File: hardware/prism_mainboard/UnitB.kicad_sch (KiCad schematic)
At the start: 1 part, among them U1 XC7Z010-1CLG400C

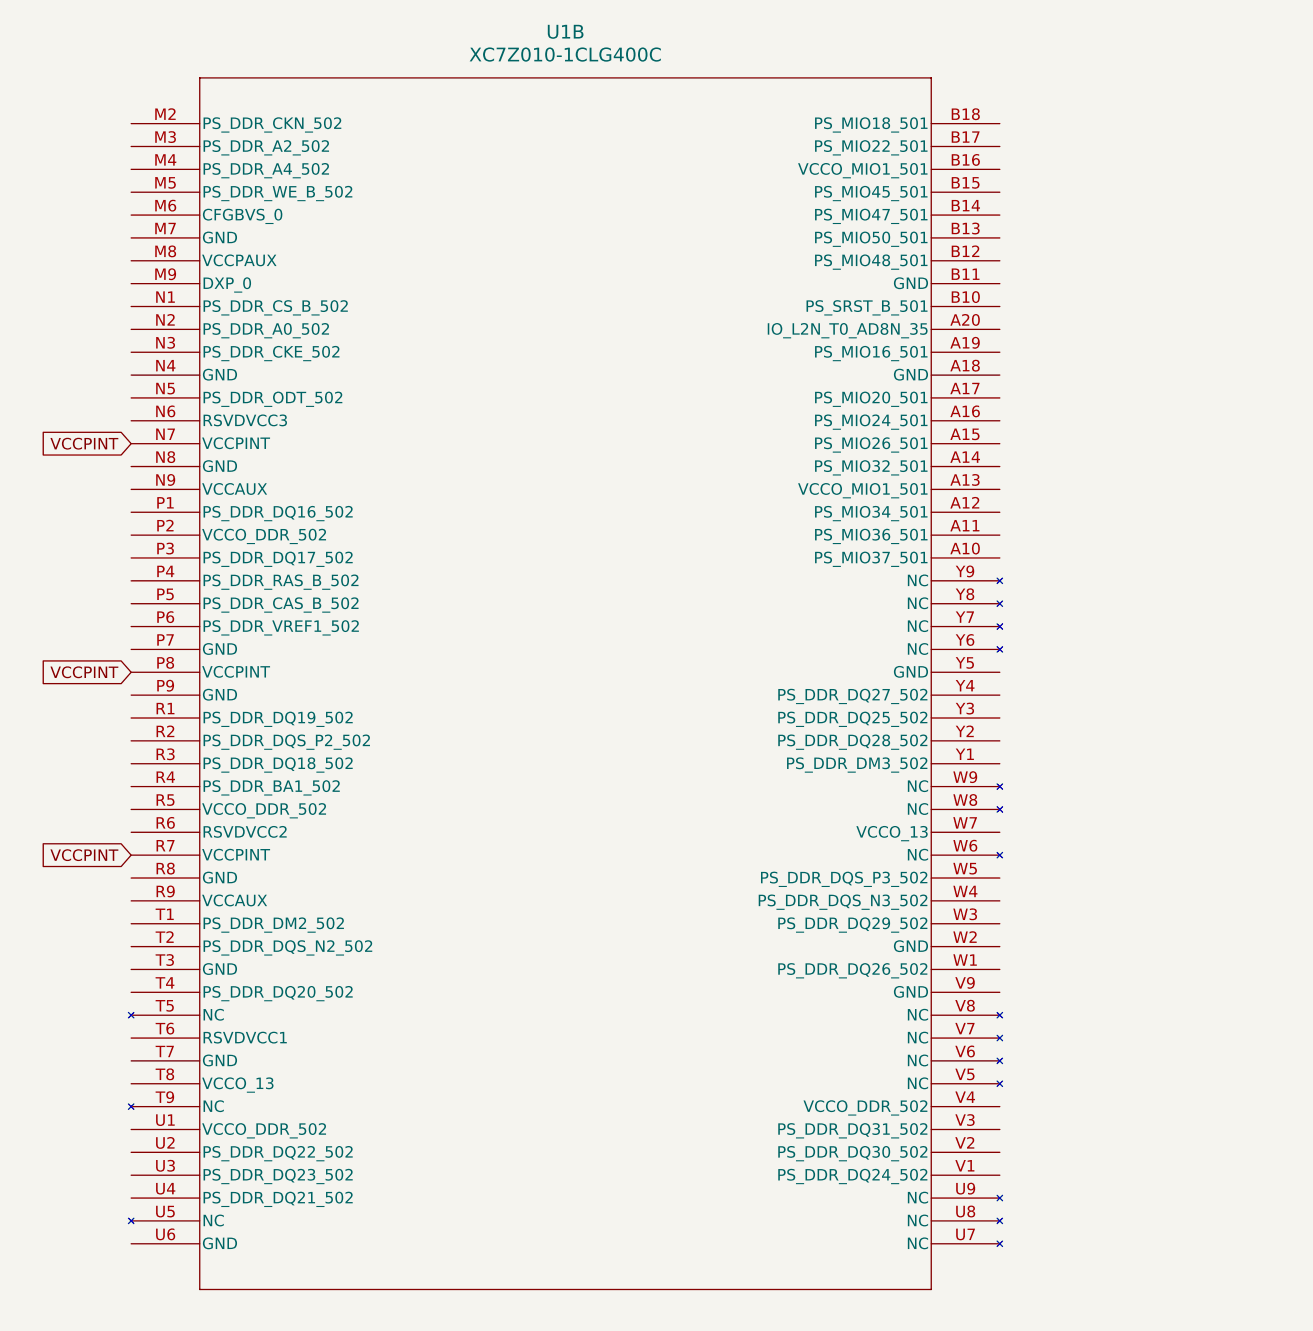
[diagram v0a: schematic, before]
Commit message: Zynq-7000 Schematic Updates
Added basic power net labels for the PL and PS portions of the FPGA.
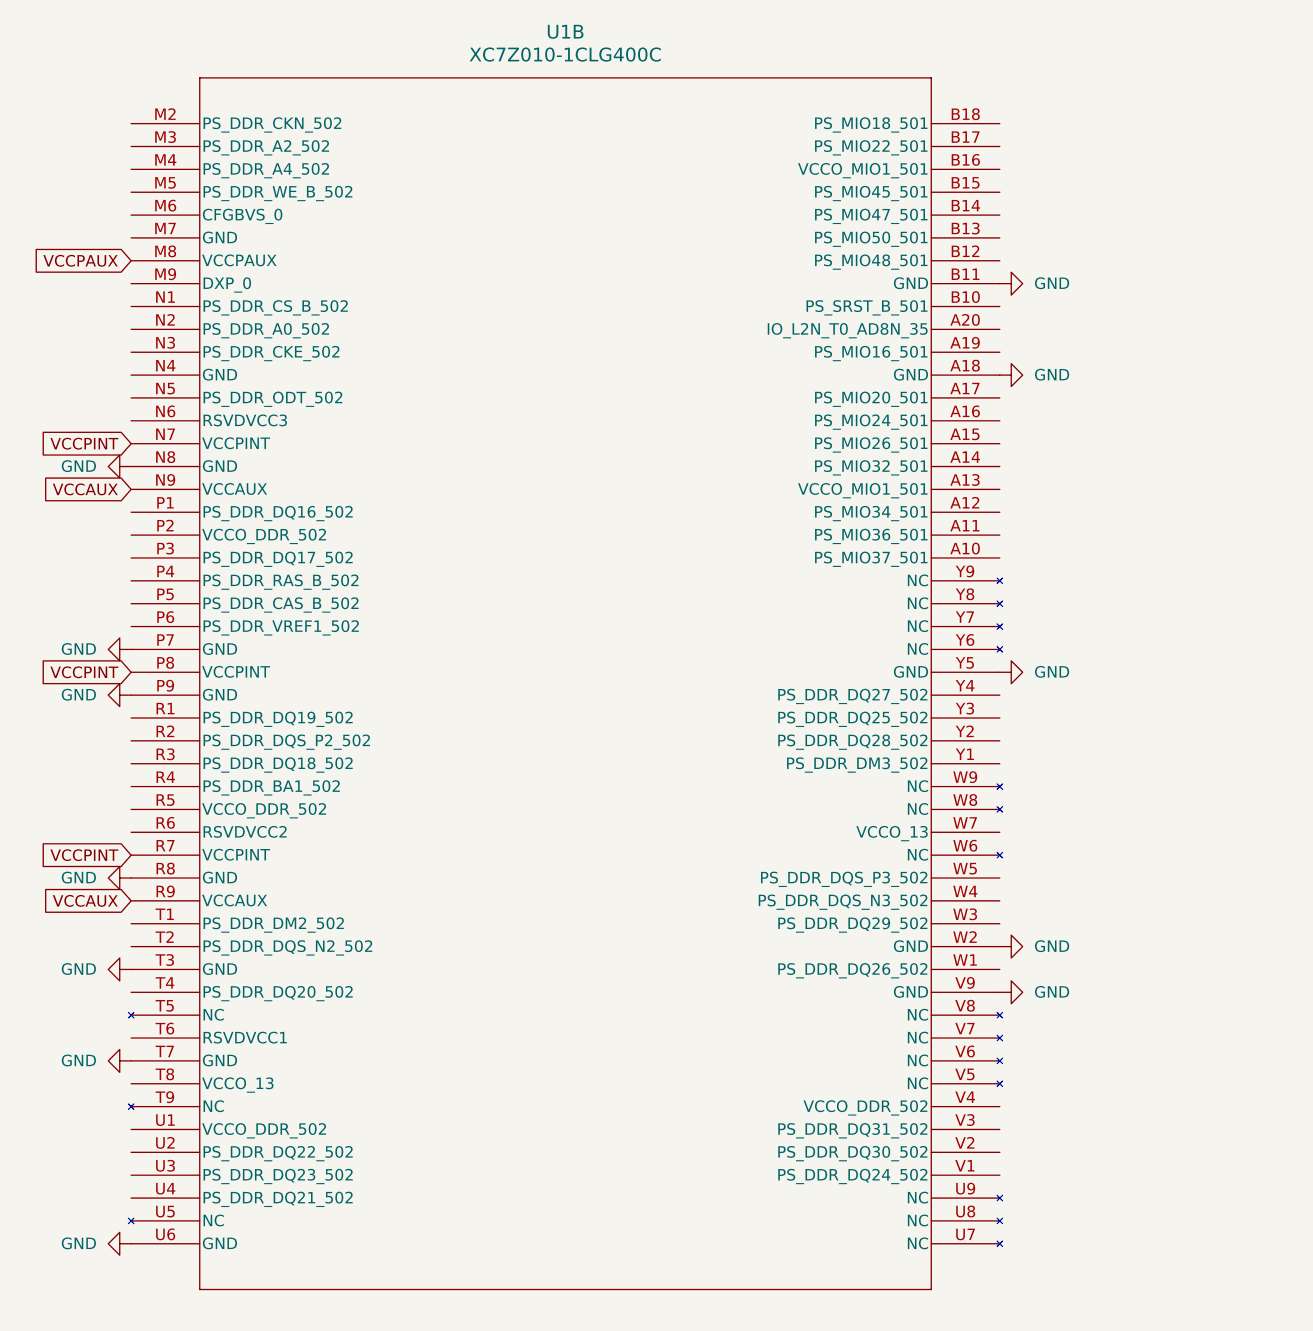
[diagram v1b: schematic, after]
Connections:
- net GND: now reaches U1.A18 (GND)
- net GND: now also U1.B11 (GND), U1.N8 (GND), U1.P7 (GND), U1.P9 (GND), U1.R8 (GND), U1.T3 (GND), U1.T7 (GND), U1.U6 (GND), U1.V9 (GND), U1.W2 (GND), U1.Y5 (GND)
- net VCCPAUX: now reaches U1.M8 (VCCPAUX)
- net VCCAUX: now reaches U1.N9 (VCCAUX)
- net VCCAUX: now also U1.R9 (VCCAUX)

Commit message: Mainboard Updates
Started a lot of the basic schematic nets like GND and Power nets. Major Change: Decided on using the XC7Z015-1CLG485I instead of the 7010 or 7020 due to the ability to use HDMI interfaces with an adapter and more LUTs. Updated schematic symbols and footprints accordingly. Added Memory, Encoder, MicroSD schematics. Added LimeSDR footprints as well. Will Try to add Power to the entire board next.
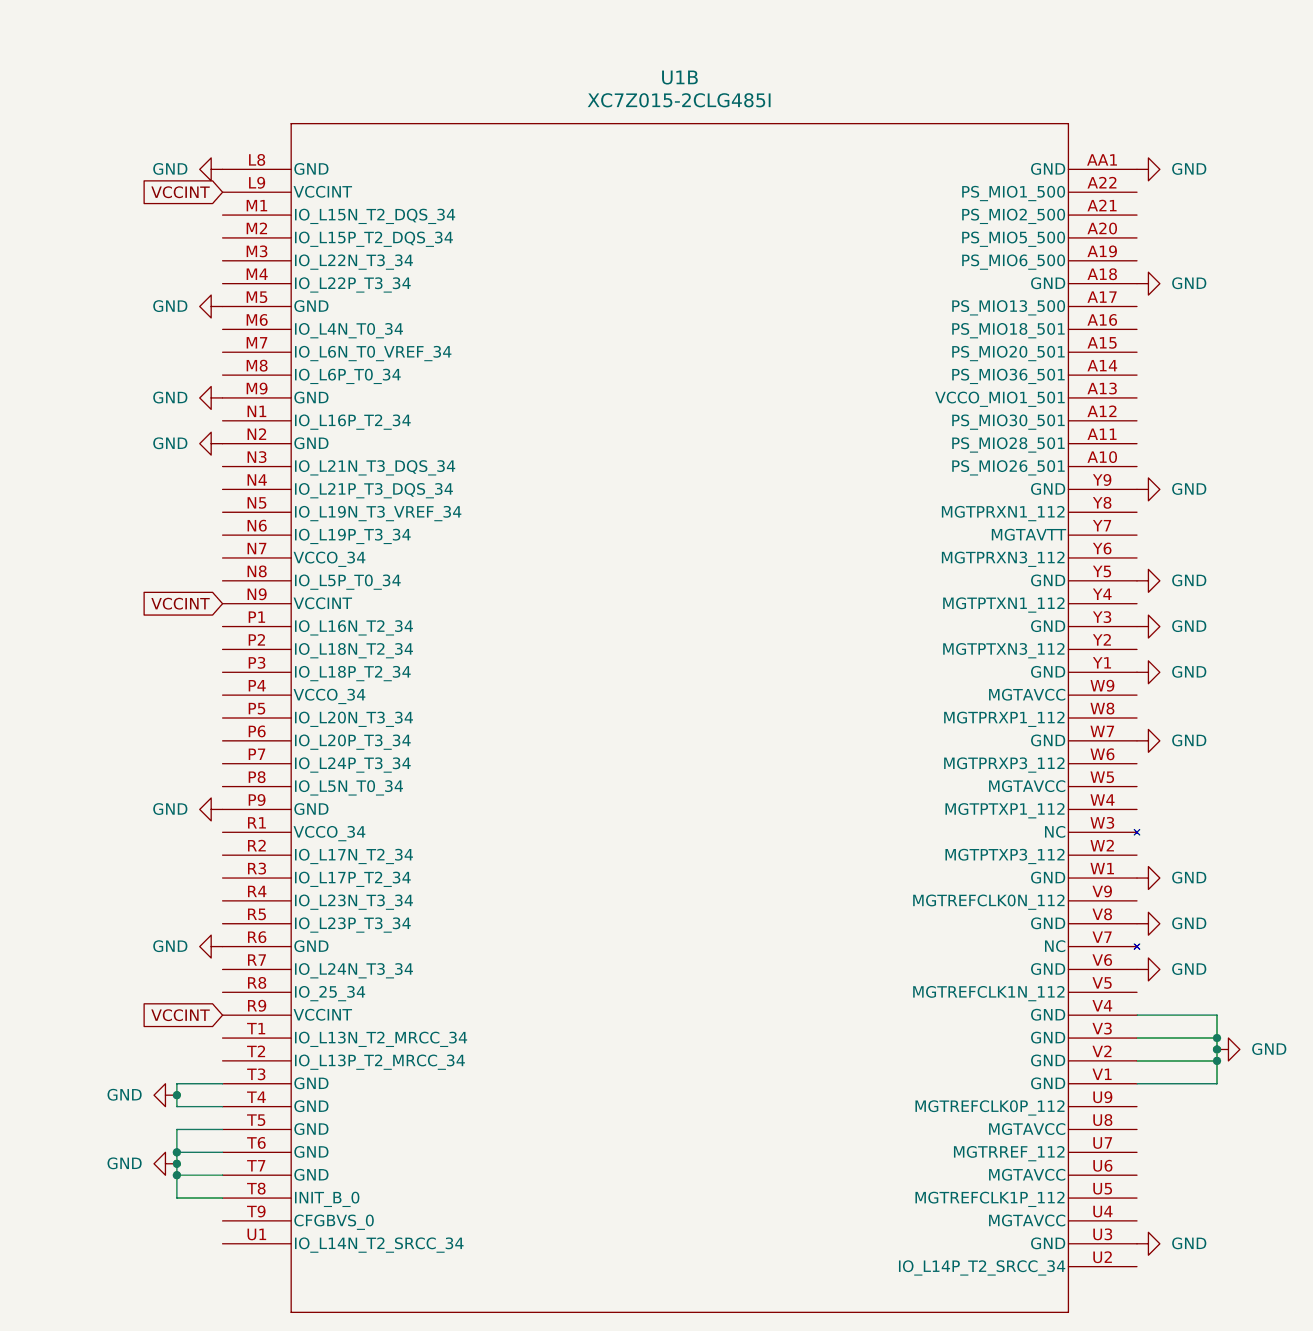
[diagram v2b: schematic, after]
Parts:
- removed U1: XC7Z010-1CLG400C, XC7Z010-1CLG400C:CLG400_XIL, symbol XC7Z010-1CLG400C:XC7Z010-1CLG400C
- added U1: XC7Z015-2CLG485I, CLG485_XIL, symbol XC7Z015-CLG485:XC7Z015-2CLG485I
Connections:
- net GND: now also U1.A18 (GND), U1.AA1 (GND), U1.L8 (GND), U1.M5 (GND), U1.M9 (GND), U1.N2 (GND), U1.P9 (GND), U1.R6 (GND), U1.T3 (GND), U1.T4 (GND), U1.T5 (GND), U1.T6 (GND), U1.T7 (GND), U1.T8 (INIT_B_0), U1.U3 (GND), U1.V1 (GND), U1.V2 (GND), U1.V3 (GND), U1.V4 (GND), U1.V6 (GND), U1.V8 (GND), U1.W1 (GND), U1.W7 (GND), U1.Y1 (GND), U1.Y3 (GND), U1.Y5 (GND), U1.Y9 (GND)
- new net VCCINT: U1.L9 (VCCINT), U1.N9 (VCCINT), U1.R9 (VCCINT)

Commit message: Schematic Updates
Updated the DDR3 DRAM to 4Gb, added a lot of nets and started updating the power and decoupling components. Updated .gitignore to avoid .mkv files.
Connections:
- net VCCO_MIO1: now reaches U1.A13 (VCCO_MIO1_501)
- net VCCO_34: now reaches U1.N7 (VCCO_34)
- net VCCO_35: now reaches U1.P4 (VCCO_34)
- net VCCO_35: now also U1.R1 (VCCO_34)
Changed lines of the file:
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@@
+		)
+	)
+	(global_label "VCCO_35"
+		(shape input)
+		(at 99.06 106.68 180)
+		(fields_autoplaced yes)
+		(effects
+			(font
+				(size 1.27 1.27)
+			)
+			(justify right)
+		)
+		(property "Intersheetrefs" "${INTERSHEET_REFS}"
+			(at 87.7291 106.68 0)
+			(hide yes)
+			(show_name no)
+			(do_not_autoplace no)
+			(effects
+				(font
+					(size 1.27 1.27)
+				)
+				(justify right)
+			)
+		)
+	)
+	(global_label "VCCO_34"
+		(shape input)
+		(at 99.06 76.2 180)
+		(fields_autoplaced yes)
+		(effects
+			(font
+				(size 1.27 1.27)
+			)
+			(justify right)
+		)
+		(property "Intersheetrefs" "${INTERSHEET_REFS}"
+			(at 87.7291 76.2 0)
+			(hide yes)
+			(show_name no)
+			(do_not_autoplace no)
+			(effects
+				(font
+					(size 1.27 1.27)
+				)
+				(justify right)
+			)
 		)
 	)
@@
 		)
 	)
+	(global_label "VCCO_MIO1"
+		(shape input)
+		(at 200.66 58.42 0)
+		(fields_autoplaced yes)
+		(effects
+			(font
+				(size 1.27 1.27)
+			)
+			(justify left)
+		)
+		(property "Intersheetrefs" "${INTERSHEET_REFS}"
+			(at 214.1681 58.42 0)
+			(hide yes)
+			(show_name no)
+			(do_not_autoplace no)
+			(effects
+				(font
+					(size 1.27 1.27)
+				)
+				(justify left)
+			)
+		)
+	)
 	(global_label "VCCINT"
 		(shape input)
@@
 			(hide yes)
 			(show_name no)
+			(do_not_autoplace no)
+			(effects
+				(font
+					(size 1.27 1.27)
+				)
+				(justify right)
+			)
+		)
+	)
+	(global_label "VCCO_35"
+		(shape input)
+		(at 99.06 91.44 180)
+		(fields_autoplaced yes)
+		(effects
+			(font
+				(size 1.27 1.27)
+			)
+			(justify right)
+		)
+		(property "Intersheetrefs" "${INTERSHEET_REFS}"
+			(at 87.7291 91.44 0)
+			(hide yes)
+			(show_name no)

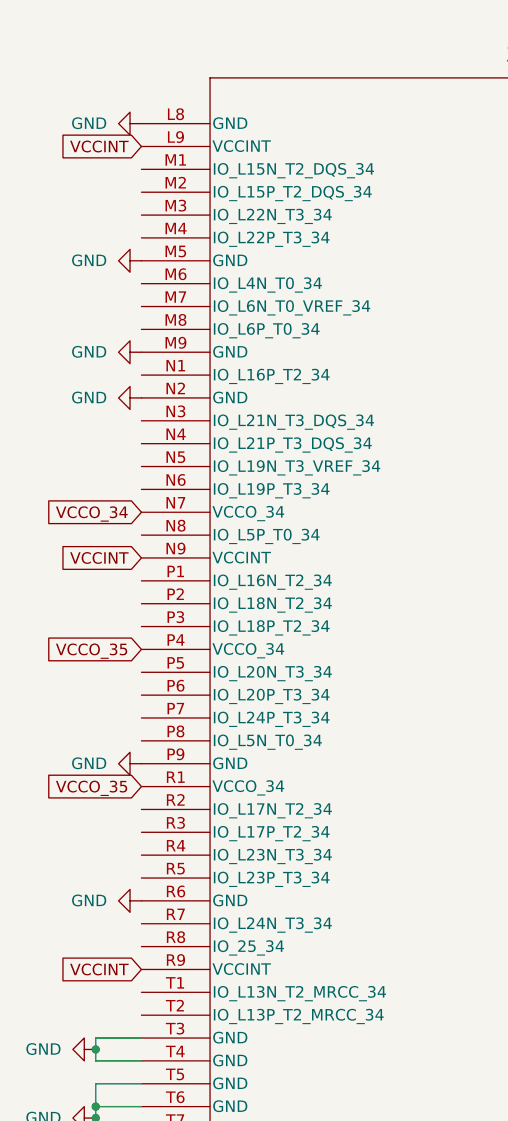
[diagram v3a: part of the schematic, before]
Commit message: Schematic Updates
Added the LMS7002M to XC7Z015 connections, atleast the preliminary data connections.
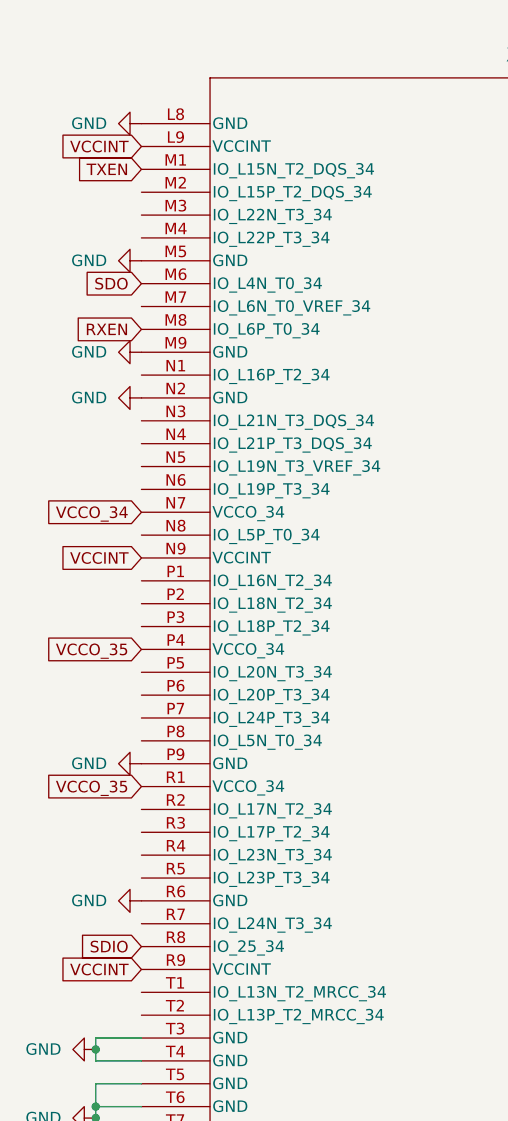
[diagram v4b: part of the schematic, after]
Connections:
- net TXEN: now reaches U1.M1 (IO_L15N_T2_DQS_34)
- net SDO: now reaches U1.M6 (IO_L4N_T0_34)
- net RXEN: now reaches U1.M8 (IO_L6P_T0_34)
- net SDIO: now reaches U1.R8 (IO_25_34)
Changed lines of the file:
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@@
+		)
+	)
+	(global_label "RXEN"
+		(shape input)
+		(at 99.06 55.88 180)
+		(fields_autoplaced yes)
+		(effects
+			(font
+				(size 1.27 1.27)
+			)
+			(justify right)
+		)
+		(property "Intersheetrefs" "${INTERSHEET_REFS}"
+			(at 91.1158 55.88 0)
+			(hide yes)
+			(show_name no)
+			(do_not_autoplace no)
+			(effects
+				(font
+					(size 1.27 1.27)
+				)
+				(justify right)
+			)
+		)
+	)
+	(global_label "SDO"
+		(shape input)
+		(at 99.06 50.8 180)
+		(fields_autoplaced yes)
+		(effects
+			(font
+				(size 1.27 1.27)
+			)
+			(justify right)
+		)
+		(property "Intersheetrefs" "${INTERSHEET_REFS}"
+			(at 92.2648 50.8 0)
+			(hide yes)
+			(show_name no)
+			(do_not_autoplace no)
+			(effects
+				(font
+					(size 1.27 1.27)
+				)
+				(justify right)
+			)
+		)
+	)
+	(global_label "TXEN"
+		(shape input)
+		(at 99.06 38.1 180)
+		(fields_autoplaced yes)
+		(effects
+			(font
+				(size 1.27 1.27)
+			)
+			(justify right)
+		)
+		(property "Intersheetrefs" "${INTERSHEET_REFS}"
+			(at 91.4182 38.1 0)
+			(hide yes)
+			(show_name no)
+			(do_not_autoplace no)
+			(effects
+				(font
+					(size 1.27 1.27)
+				)
+				(justify right)
+			)
 		)
 	)
@@
 			(hide yes)
 			(show_name no)
+			(do_not_autoplace no)
+			(effects
+				(font
+					(size 1.27 1.27)
+				)
+				(justify right)
+			)
+		)
+	)
+	(global_label "SDIO"
+		(shape input)
+		(at 99.06 124.46 180)
+		(fields_autoplaced yes)
+		(effects
+			(font
+				(size 1.27 1.27)
+			)
+			(justify right)
+		)
+		(property "Intersheetrefs" "${INTERSHEET_REFS}"
+			(at 91.66 124.46 0)
+			(hide yes)
+			(show_name no)

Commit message: Updates
Mostly Schematic updates, nothing too big. Added a few datasheets
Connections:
- net USB_D4: now reaches U1.A11 (PS_MIO28_501)
- net STP: now reaches U1.A12 (PS_MIO30_501)
- net CLKOUT: now reaches U1.A14 (PS_MIO36_501)
- net LM_RST: now reaches U1.N8 (IO_L5P_T0_34)
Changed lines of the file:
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@@
+		)
+	)
+	(global_label "LM_RST"
+		(shape input)
+		(at 99.06 78.74 180)
+		(fields_autoplaced yes)
+		(effects
+			(font
+				(size 1.27 1.27)
+			)
+			(justify right)
+		)
+		(property "Intersheetrefs" "${INTERSHEET_REFS}"
+			(at 89.1806 78.74 0)
+			(hide yes)
+			(show_name no)
+			(do_not_autoplace no)
+			(effects
+				(font
+					(size 1.27 1.27)
+				)
+				(justify right)
+			)
 		)
 	)
@@
 		)
 	)
+	(global_label "USB_D4"
+		(shape input)
+		(at 200.66 63.5 0)
+		(fields_autoplaced yes)
+		(effects
+			(font
+				(size 1.27 1.27)
+			)
+			(justify left)
+		)
+		(property "Intersheetrefs" "${INTERSHEET_REFS}"
+			(at 210.9023 63.5 0)
+			(hide yes)
+			(show_name no)
+			(do_not_autoplace no)
+			(effects
+				(font
+					(size 1.27 1.27)
+				)
+				(justify left)
+			)
+		)
+	)
 	(global_label "SDO"
 		(shape input)
@@
 		)
 	)
+	(global_label "CLKOUT"
+		(shape input)
+		(at 200.66 55.88 0)
+		(fields_autoplaced yes)
+		(effects
+			(font
+				(size 1.27 1.27)
+			)
+			(justify left)
+		)
+		(property "Intersheetrefs" "${INTERSHEET_REFS}"
+			(at 210.8419 55.88 0)
+			(hide yes)
+			(show_name no)
+			(do_not_autoplace no)
+			(effects
+				(font
+					(size 1.27 1.27)
+				)
+				(justify left)
+			)
+		)
+	)
 	(global_label "TXEN"
 		(shape input)
@@
 			)
 		)
+	)
+	(global_label "STP"
+		(shape input)
+		(at 200.66 60.96 0)
+		(fields_autoplaced yes)
+		(effects
+			(font
+				(size 1.27 1.27)
+			)
+			(justify left)
+		)
+		(property "Intersheetrefs" "${INTERSHEET_REFS}"
+			(at 207.0923 60.96 0)
+			(hide yes)
+			(show_name no)
+			(do_not_autoplace no)
+			(effects
+				(font
+					(size 1.27 1.27)
+				)
+				(justify left)
+			)
+		)
